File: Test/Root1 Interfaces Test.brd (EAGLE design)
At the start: 31.8 x 25.4 mm, 12 parts, among them J1 1X5.SEI.AB, J2 1X10.SEI.AB, J3 1X5.SEI.AT.MATE, J4 1X10SEI.AT.MATE, U1 CAT24CXX.UDFN, U2 NC7S86.SC70-5

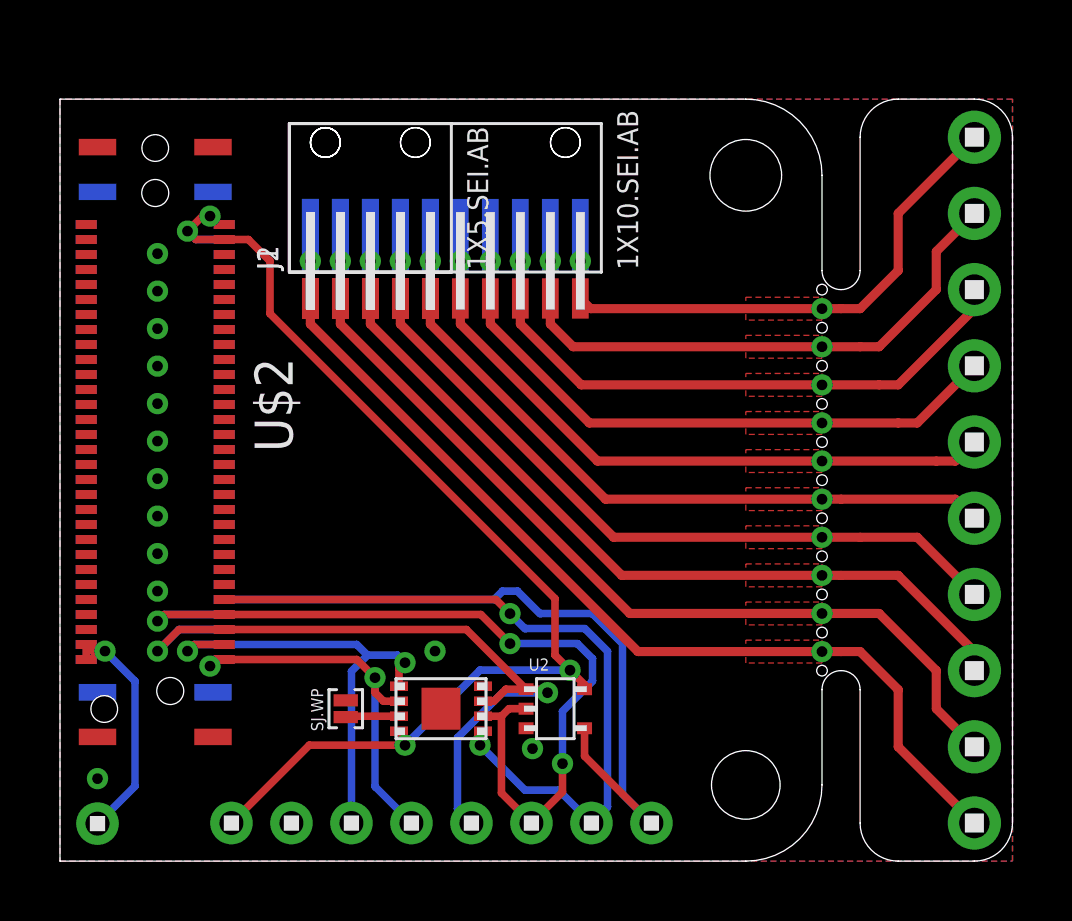
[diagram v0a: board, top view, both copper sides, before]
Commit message: Fixed routing issue in Root1 Interface Test PCB. EEPROM Address did not autoincrement...
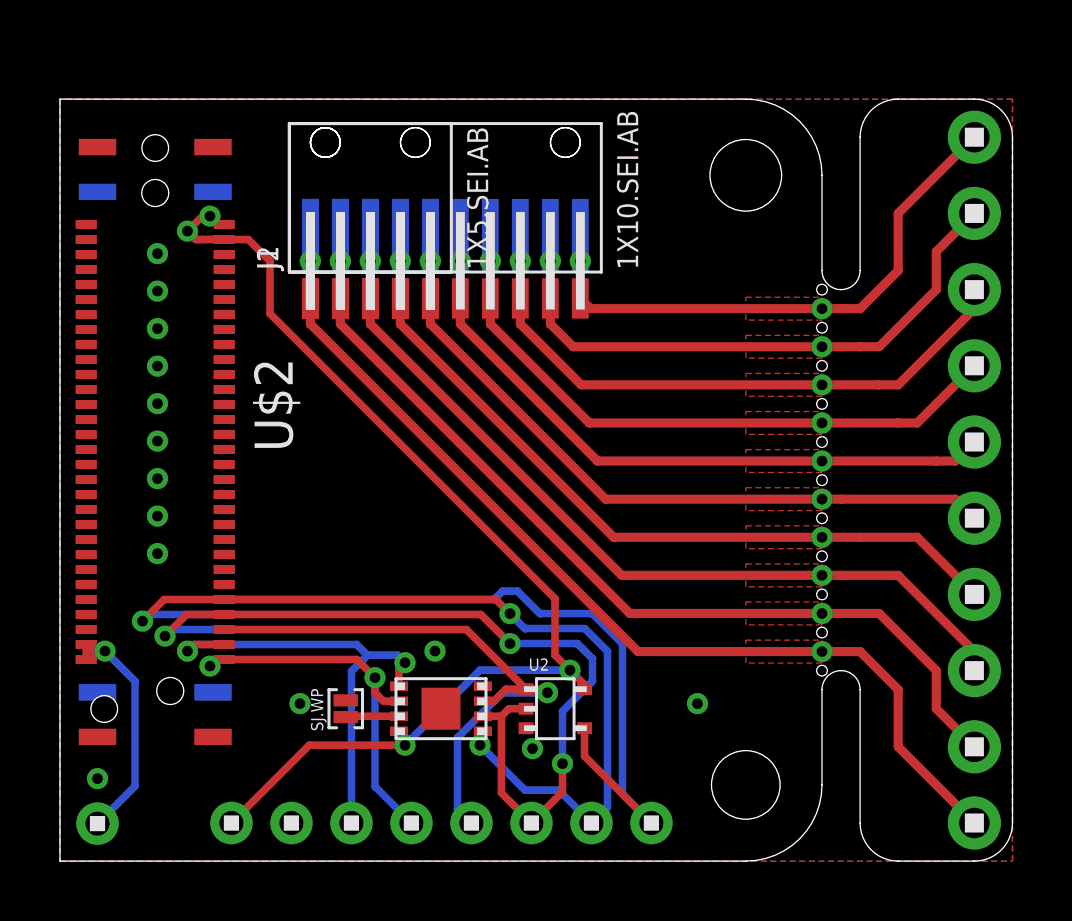
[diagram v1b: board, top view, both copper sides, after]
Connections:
- net A0: now also U$3.53
- net A1: now also U$3.55; no longer U$3.53
- net A2: no longer U$3.55
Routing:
- net A0: track 24.7 -> 30.6 mm, vias 2 -> 3
- net A2: track 25.0 -> 19.9 mm, vias 2 -> 1
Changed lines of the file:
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@@
 <setting verticaltext="up"/>
 </settings>
-<grid distance="25" unitdist="mil" unit="mil" style="dots" multiple="2" display="yes" altdistance="5" altunitdist="mil" altunit="mil"/>
+<grid distance="0.25" unitdist="mm" unit="mm" style="dots" multiple="2" display="yes" altdistance="0.05" altunitdist="mm" altunit="mm"/>
 <layers>
 <layer number="1" name="Top" color="4" fill="1" visible="yes" active="yes"/>
@@
 <layer number="27" name="tValues" color="7" fill="1" visible="no" active="yes"/>
 <layer number="28" name="bValues" color="7" fill="1" visible="no" active="yes"/>
-<layer number="29" name="tStop" color="7" fill="3" visible="yes" active="yes"/>
-<layer number="30" name="bStop" color="7" fill="6" visible="yes" active="yes"/>
+<layer number="29" name="tStop" color="7" fill="3" visible="no" active="yes"/>
+<layer number="30" name="bStop" color="7" fill="6" visible="no" active="yes"/>
 <layer number="31" name="tCream" color="7" fill="4" visible="no" active="yes"/>
 <layer number="32" name="bCream" color="7" fill="5" visible="no" active="yes"/>
@@
 <via x="3.25" y="11.5" extent="1-16" drill="0.3556"/>
 <via x="3.25" y="10.25" extent="1-16" drill="0.3556"/>
-<via x="3.25" y="9" extent="1-16" drill="0.3556"/>
 <via x="1.25" y="2.75" extent="1-16" drill="0.3556"/>
-<wire x1="15.535" y1="4.43" x2="14.1" y2="5.83" width="0" layer="19" extent="1-1"/>
-<wire x1="9.525" y1="5.3594" x2="12.7" y2="5.08" width="0" layer="19" extent="1-1"/>
+<via x="8" y="5.25" extent="1-16" drill="0.3556"/>
+<via x="21.25" y="5.25" extent="1-16" drill="0.3556"/>
 </signal>
 <signal name="N$30">
@@
 <wire x1="15" y1="8.25" x2="14.53" y2="8.72" width="0.254" layer="1"/>
 <wire x1="14.53" y1="8.72" x2="5.475" y2="8.72" width="0.254" layer="1"/>
+<contactref element="U$3" pad="53"/>
+<wire x1="5.475" y1="8.72" x2="3.47" y2="8.72" width="0.254" layer="1"/>
+<wire x1="3.47" y1="8.72" x2="2.75" y2="8" width="0.254" layer="1"/>
+<via x="2.75" y="8" extent="1-16" drill="0.3556"/>
+<wire x1="2.75" y1="8" x2="2.97" y2="8.22" width="0.254" layer="16"/>
+<wire x1="2.97" y1="8.22" x2="5.475" y2="8.22" width="0.254" layer="16"/>
 </signal>
 <signal name="A1">
@@
 <wire x1="14.715" y1="4.83" x2="14.715" y2="2.27" width="0.254" layer="1"/>
 <wire x1="14.715" y1="2.27" x2="15.715" y2="1.27" width="0.254" layer="1"/>
-<contactref element="U$3" pad="53"/>
 <contactref element="U$2" pad="53"/>
-<wire x1="5.475" y1="8.22" x2="3.47" y2="8.22" width="0.254" layer="16"/>
-<wire x1="3.47" y1="8.22" x2="3.25" y2="8" width="0.254" layer="16"/>
-<via x="3.25" y="8" extent="1-16" drill="0.3556"/>
-<wire x1="3.25" y1="8" x2="3.47" y2="8.22" width="0.254" layer="1"/>
-<wire x1="3.47" y1="8.22" x2="5.475" y2="8.22" width="0.254" layer="1"/>
+<via x="3.5" y="7.5" extent="1-16" drill="0.3556"/>
+<wire x1="3.5" y1="7.5" x2="4.22" y2="8.22" width="0.254" layer="1"/>
+<wire x1="4.22" y1="8.22" x2="5.475" y2="8.22" width="0.254" layer="1"/>
 <wire x1="5.475" y1="8.22" x2="14.03" y2="8.22" width="0.254" layer="1"/>
 <wire x1="14.03" y1="8.22" x2="15" y2="7.25" width="0.254" layer="1"/>
@@
 <wire x1="16.75" y1="3.25" x2="16.75" y2="2.305" width="0.254" layer="1"/>
 <wire x1="16.75" y1="2.305" x2="15.715" y2="1.27" width="0.254" layer="1"/>
+<contactref element="U$3" pad="55"/>
+<wire x1="5.475" y1="7.72" x2="3.72" y2="7.72" width="0.254" layer="16"/>
+<wire x1="3.72" y1="7.72" x2="3.5" y2="7.5" width="0.254" layer="16"/>
 </signal>
 <signal name="A2">
@@
 <wire x1="13.25" y1="4.115" x2="13.25" y2="1.735" width="0.254" layer="16"/>
 <wire x1="13.25" y1="1.735" x2="13.715" y2="1.27" width="0.254" layer="16"/>
-<contactref element="U$3" pad="55"/>
 <contactref element="U$2" pad="55"/>
-<wire x1="5.475" y1="7.72" x2="3.97" y2="7.72" width="0.254" layer="1"/>
-<wire x1="3.97" y1="7.72" x2="3.25" y2="7" width="0.254" layer="1"/>
-<via x="3.25" y="7" extent="1-16" drill="0.3556"/>
-<wire x1="3.25" y1="7" x2="3.97" y2="7.72" width="0.254" layer="16"/>
-<wire x1="3.97" y1="7.72" x2="5.475" y2="7.72" width="0.254" layer="16"/>
 <wire x1="15.535" y1="5.73" x2="13.545" y2="7.72" width="0.254" layer="1"/>
 <wire x1="13.545" y1="7.72" x2="5.475" y2="7.72" width="0.254" layer="1"/>
